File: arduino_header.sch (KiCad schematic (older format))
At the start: 4 parts, among them J3 Conn_01x08, J4 Conn_01x06, J5 Conn_01x10, J6 Conn_01x08

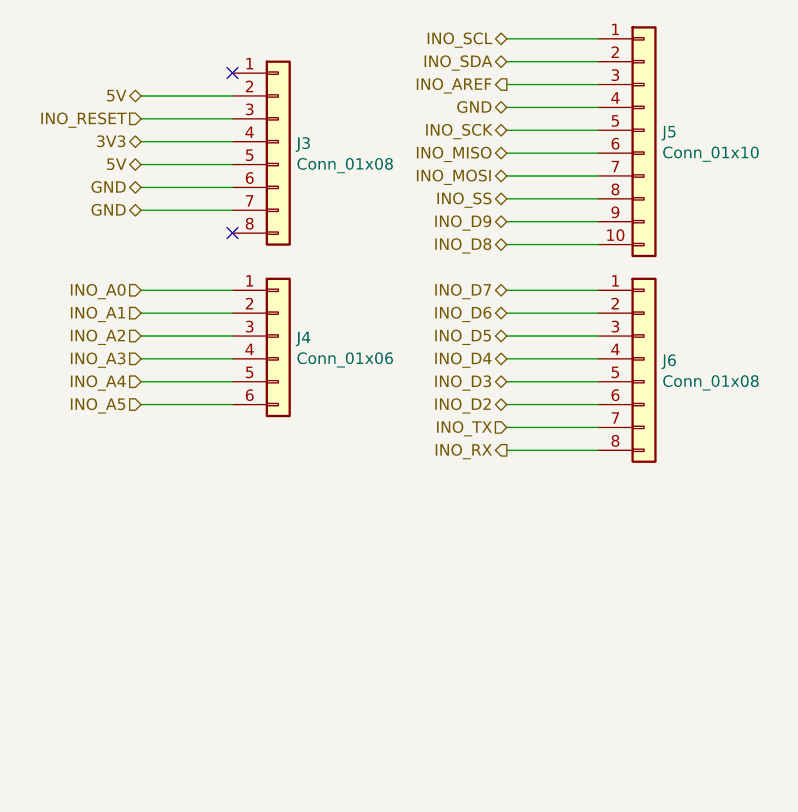
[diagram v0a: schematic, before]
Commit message: 7-17 VIN Power PIN Header moved to the left for better compatibility with extension boards. Added 0 Ohm resistors for optional desoldering of quad-SPI wires. USB power jumper moved more to the side of the board. Arduino Header decoupling capacitors moved to arduino header sheet.
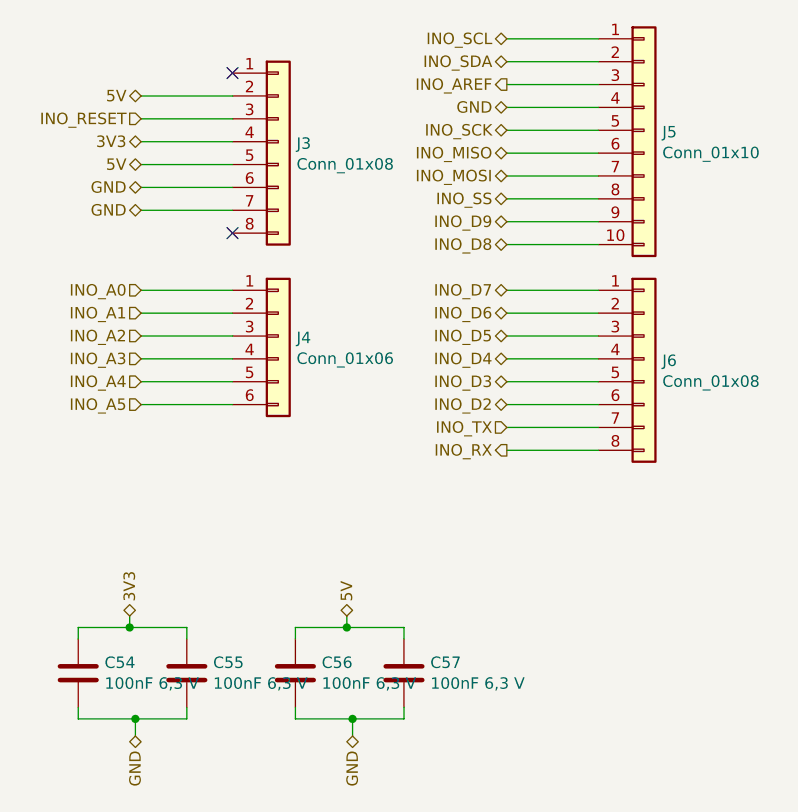
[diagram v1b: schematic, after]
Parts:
- added C54, C55, C56, C57: 100nF 6,3 V, Capacitor_SMD:C_0603_1608Metric, symbol Device:C
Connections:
- net 3V3: now also C54.1, C55.1
- net 5V: now also C56.1, C57.1
- net GND: now also C54.2, C55.2, C56.2, C57.2
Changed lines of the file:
@@
 Text HLabel 4250 1800 0    50   Output ~ 0
 INO_AREF
+$Comp
+L Device:C C?
+U 1 1 5F1FEE68
+P 2850 4375
+AR Path="/5CAB7CD4/5F1FEE68" Ref="C?"  Part="1"
+AR Path="/5CB5889B/5F1FEE68" Ref="C?"  Part="1"
+AR Path="/5ED96D61/5F1FEE68" Ref="C?"  Part="1"
+AR Path="/5ED96D61/5EE3E16B/5F1FEE68" Ref="C55"  Part="1"
+F 0 "C55" H 2965 4421 50  0000 L CNN
+F 1 "100nF 6,3 V" H 2965 4330 50  0000 L CNN
+F 2 "Capacitor_SMD:C_0603_1608Metric" H 2888 4225 50  0001 C CNN
+F 3 "~" H 2850 4375 50  0001 C CNN
+F 4 "CAP CER 0.1UF 50V X7R 0603" H -2800 -2750 50  0001 C CNN "Description"
+F 5 "1276-1000-1-ND" H -2800 -2750 50  0001 C CNN "Digikey"
+F 6 "Samsung Electro-Mechanics" H -2800 -2750 50  0001 C CNN "Mfg Name"
+F 7 "CL10B104KB8NNNC" H -2800 -2750 50  0001 C CNN "Mfg Part Num"
+F 8 "Any" H -2800 -2750 50  0001 C CNN "Spec"
+	1    2850 4375
+	1    0    0    -1
+$EndComp
+Wire Wire Line
+	2375 4525 2375 4575
+Wire Wire Line
+	2375 4575 2625 4575
+Wire Wire Line
+	2850 4575 2850 4525
+Wire Wire Line
+	2625 4650 2625 4575
+Connection ~ 2625 4575
+Wire Wire Line
+	2625 4575 2850 4575
+Wire Wire Line
+	2375 4225 2375 4175
+Wire Wire Line
+	2375 4175 2600 4175
+Wire Wire Line
+	2850 4175 2850 4225
+Wire Wire Line
+	2600 4125 2600 4175
+Connection ~ 2600 4175
+Wire Wire Line
+	2600 4175 2850 4175
+$Comp
+L Device:C C?
+U 1 1 5F1FEE7F
+P 3325 4375
+AR Path="/5CAB7CD4/5F1FEE7F" Ref="C?"  Part="1"
+AR Path="/5CB5889B/5F1FEE7F" Ref="C?"  Part="1"
+AR Path="/5ED96D61/5F1FEE7F" Ref="C?"  Part="1"
+AR Path="/5ED96D61/5EE3E16B/5F1FEE7F" Ref="C56"  Part="1"
+F 0 "C56" H 3440 4421 50  0000 L CNN
+F 1 "100nF 6,3 V" H 3440 4330 50  0000 L CNN
+F 2 "Capacitor_SMD:C_0603_1608Metric" H 3363 4225 50  0001 C CNN
+F 3 "~" H 3325 4375 50  0001 C CNN
+F 4 "CAP CER 0.1UF 50V X7R 0603" H -2800 -2750 50  0001 C CNN "Description"
+F 5 "1276-1000-1-ND" H -2800 -2750 50  0001 C CNN "Digikey"
+F 6 "Samsung Electro-Mechanics" H -2800 -2750 50  0001 C CNN "Mfg Name"
+F 7 "CL10B104KB8NNNC" H -2800 -2750 50  0001 C CNN "Mfg Part Num"
+F 8 "Any" H -2800 -2750 50  0001 C CNN "Spec"
+	1    3325 4375
+	1    0    0    -1
+$EndComp
+$Comp
+L Device:C C?
+U 1 1 5F1FEE8A
+P 3800 4375
+AR Path="/5CAB7CD4/5F1FEE8A" Ref="C?"  Part="1"
+AR Path="/5CB5889B/5F1FEE8A" Ref="C?"  Part="1"
+AR Path="/5ED96D61/5F1FEE8A" Ref="C?"  Part="1"
+AR Path="/5ED96D61/5EE3E16B/5F1FEE8A" Ref="C57"  Part="1"
+F 0 "C57" H 3915 4421 50  0000 L CNN
+F 1 "100nF 6,3 V" H 3915 4330 50  0000 L CNN
+F 2 "Capacitor_SMD:C_0603_1608Metric" H 3838 4225 50  0001 C CNN
+F 3 "~" H 3800 4375 50  0001 C CNN
+F 4 "CAP CER 0.1UF 50V X7R 0603" H -2800 -2750 50  0001 C CNN "Description"
+F 5 "1276-1000-1-ND" H -2800 -2750 50  0001 C CNN "Digikey"
+F 6 "Samsung Electro-Mechanics" H -2800 -2750 50  0001 C CNN "Mfg Name"
+F 7 "CL10B104KB8NNNC" H -2800 -2750 50  0001 C CNN "Mfg Part Num"
+F 8 "Any" H -2800 -2750 50  0001 C CNN "Spec"
+	1    3800 4375
+	1    0    0    -1
+$EndComp
+Wire Wire Line
+	3325 4525 3325 4575
+Wire Wire Line
+	3325 4575 3575 4575
+Wire Wire Line
+	3800 4575 3800 4525
+Wire Wire Line
+	3575 4650 3575 4575
+Connection ~ 3575 4575
+Wire Wire Line
+	3575 4575 3800 4575
+Wire Wire Line
+	3325 4225 3325 4175
+Wire Wire Line
+	3325 4175 3550 4175
+Wire Wire Line
+	3800 4175 3800 4225
+Wire Wire Line
+	3550 4125 3550 4175
+Connection ~ 3550 4175
+Wire Wire Line
+	3550 4175 3800 4175
+$Comp
+L Device:C C?
+U 1 1 5F1FEEA1
+P 2375 4375
+AR Path="/5CAB7CD4/5F1FEEA1" Ref="C?"  Part="1"
+AR Path="/5CB5889B/5F1FEEA1" Ref="C?"  Part="1"
+AR Path="/5ED96D61/5F1FEEA1" Ref="C?"  Part="1"
+AR Path="/5ED96D61/5EE3E16B/5F1FEEA1" Ref="C54"  Part="1"
+F 0 "C54" H 2490 4421 50  0000 L CNN
+F 1 "100nF 6,3 V" H 2490 4330 50  0000 L CNN
+F 2 "Capacitor_SMD:C_0603_1608Metric" H 2413 4225 50  0001 C CNN
+F 3 "~" H 2375 4375 50  0001 C CNN
+F 4 "CAP CER 0.1UF 50V X7R 0603" H -2800 -2750 50  0001 C CNN "Description"
+F 5 "1276-1000-1-ND" H -2800 -2750 50  0001 C CNN "Digikey"
+F 6 "Samsung Electro-Mechanics" H -2800 -2750 50  0001 C CNN "Mfg Name"
+F 7 "CL10B104KB8NNNC" H -2800 -2750 50  0001 C CNN "Mfg Part Num"
+F 8 "Any" H -2800 -2750 50  0001 C CNN "Spec"
+	1    2375 4375
+	1    0    0    -1
+$EndComp
+Text HLabel 2600 4125 1    50   BiDi ~ 0
+3V3
+Text HLabel 3550 4125 1    50   BiDi ~ 0
+5V
+Text HLabel 3575 4650 3    50   BiDi ~ 0
+GND
+Text HLabel 2625 4650 3    50   BiDi ~ 0
+GND
 $EndSCHEMATC
